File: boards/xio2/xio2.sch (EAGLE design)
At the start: 281 parts, among them J1 12401598E4#2A, Q1 BSS138, Q2 BSS138, X1 MINI-USB-UX60-MB-5ST, Y2 NX3225SA-12.000MHZ-STD-CSR-1

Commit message: Start work on the BGA STMH7
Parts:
- removed U$1: STM32H743XIH6, sjg-stm32:STM32H743XIH6
- added C99: 2.2uF, rcl:C-EUC0402K
- added R91, R92, R93: 33R, rcl:R-EU_R0402
- added TP14: (no value), microbuilder:TESTPOINTROUND0.5MM
- XIO: value STM32F429B-XIO -> STM32H743-XIO; device sjg-stm32:STM32F429B-XIO -> sjg-stm32:STM32H743-XIO
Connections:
- removed net N$100: U$1.P$35, U$1.P$36, U$1.P$37, U$1.P$38, U$1.P$39, U$1.P$40, U$1.P$41, U$1.P$42
- removed net N$101: U$1.P$52, U$1.P$53, U$1.P$55, U$1.P$56, U$1.P$57, U$1.P$58
- removed net N$102: U$1.P$69, U$1.P$70, U$1.P$71, U$1.P$72, U$1.P$73, U$1.P$74, U$1.P$75
- new net XIO_VCAP3: C99.1, XIO-POWER.VCAP3@A7
- new net XSPI_2_MISO: R75.2
- new net XSPI_2_MOSI: XIO-XSPI.PB15@T15
- new net XSPI_2_SCK: XIO-XSPI.PB13@U14
- net !RESET!: now also XIO-POWER.!RST!@K1; no longer XIO-POWER.!RST!@34
- net !SDRAM_CAS!: now also XIO-SDRAM.PG15@D6; no longer XIO-SDRAM.PG15@191
- net !SDRAM_RAS!: now also XIO-SDRAM.PF11@T7; no longer XIO-SDRAM.PF11@70
- net !SDRAM_WE!: now also XIO-SDRAM.PH5@P4; no longer XIO-SDRAM.PH5@49
- net +3V3: now also XIO-POWER.VBAT@B1, XIO-POWER.VDD33USB@F17, XIO-POWER.VDD@E11, XIO-POWER.VDD@E6, XIO-POWER.VDD@E9, XIO-POWER.VDD@F5, XIO-POWER.VDD@G13, XIO-POWER.VDD@G5, XIO-POWER.VDD@H13, XIO-POWER.VDD@H5, XIO-POWER.VDD@J13, XIO-POWER.VDD@K13, XIO-POWER.VDD@K5, XIO-POWER.VDD@L13, XIO-POWER.VDD@L5, XIO-POWER.VDD@M13, XIO-POWER.VDD@M5, XIO-POWER.VDD@N10, XIO-POWER.VDD@N11, XIO-POWER.VDD@N12, XIO-POWER.VDD@N7, XIO-POWER.VDD@N8, XIO-POWER.VDD@P17, XIO-POWER.VDDLDO@A6, XIO-POWER.VDDLDO@C17, XIO-POWER.VDDLDO@U12; no longer XIO-POWER.VBAT@6, XIO-POWER.VDD@103, XIO-POWER.VDD@115, XIO-POWER.VDD@124, XIO-POWER.VDD@15, XIO-POWER.VDD@150, XIO-POWER.VDD@158, XIO-POWER.VDD@171, XIO-POWER.VDD@185, XIO-POWER.VDD@204, XIO-POWER.VDD@26, XIO-POWER.VDD@39, XIO-POWER.VDD@52, XIO-POWER.VDD@59, XIO-POWER.VDD@73, XIO-POWER.VDD@83, XIO-POWER.VDD@94, XIO-POWER.VDDUSB@137
- net AGND: now also XIO-POWER.VREF-@N1, XIO-POWER.VSSA@P1
- net ARCH0: now also XIO-CFG.PG2@H16; no longer XIO-CFG.PG2@129
- net ARCH1: now also XIO-CFG.PG3@H15; no longer XIO-CFG.PG3@130
- net ARCH2: now also XIO-CFG.PG6@G15; no longer XIO-CFG.PG6@133
- net ARCH3: now also XIO-CFG.PG7@F16; no longer XIO-CFG.PG7@134
- net AUX_CTS: now also XIO-UART.PD11@R15; no longer XIO-SERIAL.PB13@105
- net AUX_RTS: now also XIO-UART.PD12@R16; no longer XIO-SERIAL.PB14@106
- net AUX_RX: now also XIO-UART.PB11@P12; no longer XIO-SERIAL.PB11@91
- net AUX_TX: now also XIO-UART.PB10@P11; no longer XIO-SERIAL.PB10@90
- net BOOT0: now also XIO-POWER.BOOT0@E8; no longer XIO-POWER.BOOT0@197
- net GND: now also C99.2, XIO-NC.F1, XIO-NC.F2, XIO-NC.G2, XIO-POWER.VSS@A1, XIO-POWER.VSS@A17, XIO-POWER.VSS@B2, XIO-POWER.VSS@B6, XIO-POWER.VSS@C10, XIO-POWER.VSS@C13, XIO-POWER.VSS@C16, XIO-POWER.VSS@G10, XIO-POWER.VSS@G11, XIO-POWER.VSS@G16, XIO-POWER.VSS@G7, XIO-POWER.VSS@G8, XIO-POWER.VSS@G9, XIO-POWER.VSS@H10, XIO-POWER.VSS@H11, XIO-POWER.VSS@H7, XIO-POWER.VSS@H8, XIO-POWER.VSS@H9, XIO-POWER.VSS@J10, XIO-POWER.VSS@J11, XIO-POWER.VSS@J16, XIO-POWER.VSS@J17, XIO-POWER.VSS@J3, XIO-POWER.VSS@J7, XIO-POWER.VSS@J8, XIO-POWER.VSS@J9, XIO-POWER.VSS@K10, XIO-POWER.VSS@K11, XIO-POWER.VSS@K15, XIO-POWER.VSS@K7, XIO-POWER.VSS@K8, XIO-POWER.VSS@K9, XIO-POWER.VSS@L10, XIO-POWER.VSS@L11, XIO-POWER.VSS@L15, XIO-POWER.VSS@L7, XIO-POWER.VSS@L8, XIO-POWER.VSS@L9, XIO-POWER.VSS@M15, XIO-POWER.VSS@N16, XIO-POWER.VSS@R4, XIO-POWER.VSS@R8, XIO-POWER.VSS@T12, XIO-POWER.VSS@U1, XIO-POWER.VSS@U17; no longer XIO-POWER.VSS@114, XIO-POWER.VSS@125, XIO-POWER.VSS@136, XIO-POWER.VSS@14, XIO-POWER.VSS@149, XIO-POWER.VSS@170, XIO-POWER.VSS@184, XIO-POWER.VSS@202, XIO-POWER.VSS@25, XIO-POWER.VSS@51, XIO-POWER.VSS@60, XIO-POWER.VSS@72, XIO-POWER.VSS@82, XIO-POWER.VSS@93, XIO-POWER.VSSA@40
- net LCD_B0: now also XIO-LCD.PJ12@D11; no longer XIO-VGA.PJ12@174
- net LCD_B1: now also XIO-LCD.PJ13@E10; no longer XIO-VGA.PJ13@175
- net LCD_B2: now also XIO-LCD.PJ14@D10; no longer XIO-VGA.PJ14@176
- net LCD_B3: now also XIO-LCD.PJ15@B10; no longer XIO-VGA.PJ15@177
- net LCD_B4: now also XIO-LCD.PK3@C8; no longer XIO-VGA.PK3@186
- net LCD_B5: now also XIO-LCD.PK4@B8; no longer XIO-VGA.PK4@187
- net LCD_B6: now also XIO-LCD.PK5@A8; no longer XIO-VGA.PK5@188
- net LCD_B7: now also XIO-LCD.PK6@C7; no longer XIO-VGA.PK6@189
- net LCD_G0: now also XIO-LCD.PJ7@N14; no longer XIO-VGA.PJ7@119
- net LCD_G1: now also XIO-LCD.PJ8@N13; no longer XIO-VGA.PJ8@120
- net LCD_G2: now also XIO-LCD.PJ9@M14; no longer XIO-VGA.PJ9@121
- net LCD_G3: now also XIO-LCD.PJ10@L14; no longer XIO-VGA.PJ10@122
- net LCD_G4: now also XIO-LCD.PJ11@K14; no longer XIO-VGA.PJ11@123
- net LCD_G5: now also XIO-LCD.PK0@J14; no longer XIO-VGA.PK0@126
- net LCD_G6: now also XIO-LCD.PK1@J15; no longer XIO-VGA.PK1@127
- net LCD_G7: now also XIO-LCD.PK2@H17; no longer XIO-VGA.PK2@128
- net LCD_HS: now also XIO-LCD.PI13@H2; no longer XIO-VGA.PI13@20
- net LCD_R0: now also XIO-LCD.PI15@P5; no longer XIO-VGA.PI15@64
- net LCD_R1: now also XIO-LCD.PJ0@N6; no longer XIO-VGA.PJ0@65
- net LCD_R2: now also XIO-LCD.PJ1@P6; no longer XIO-VGA.PJ1@66
- net LCD_R3: now also XIO-LCD.PJ2@T6; no longer XIO-VGA.PJ2@67
- net LCD_R4: now also XIO-LCD.PJ3@U6; no longer XIO-VGA.PJ3@68
- net LCD_R5: now also XIO-LCD.PJ4@U7; no longer XIO-VGA.PJ4@69
- net LCD_R6: now also XIO-LCD.PJ5@R12; no longer XIO-VGA.PJ5@95
- net LCD_R7: now also XIO-LCD.PJ6@N15; no longer XIO-VGA.PJ6@118
- net LCD_VS: now also XIO-LCD.PI12@H1; no longer XIO-VGA.PI12@19
- net MCU_CTS: now also XIO-UART.PD3@B12; no longer XIO-SERIAL.PD3@167
- net MCU_RTS: now also XIO-UART.PD4@A12; no longer XIO-SERIAL.PD4@168
- net MCU_RX: now also XIO-UART.PD6@B11; no longer XIO-SERIAL.PD6@172
- net MCU_TX: now also XIO-UART.PD5@A11; no longer XIO-SERIAL.PD5@169
- net MEM0: now also XIO-CFG.PG10@A9; no longer XIO-CFG.PG10@179
- net MEM1: now also XIO-CFG.PG11@B9; no longer XIO-CFG.PG11@180
- net N$1: now also XIO-POWER.PH1@J2; no longer XIO-POWER.PH1@33
- net N$13: now also XIO-LED.PC13@E3; no longer XIO-LED.PD11@111
- net N$14: now also XIO-LED.PC14@C2; no longer XIO-LED.PD12@112
- net N$15: now also XIO-LED.PC15@C1; no longer XIO-LED.PD13@113
- net N$2: now also XIO-POWER.PH0@J1; no longer XIO-POWER.PH0@32
- net N$57: now also XIO-SPI.PE2@C3; no longer XIO-SPI.PE2@1
- net N$61: now also XIO-SPI.PE6@E5; no longer XIO-SPI.PE6@5
- net N$64: now also XIO-USB.PA15@A14; no longer XIO-USB.PA15@160
- net N$65: now also XIO-USB.PD7@C11; no longer XIO-USB.PD7@173
- net N$72: now also XIO-XSPI.PB14@U15; no longer XIOG$1.PB4@193
- net N$73: now also XIO-XSPI.PB4@B7; no longer XIOG$1.PF8@29
- net N$74: now also XIO-XSPI.PF7@K3; no longer XIOG$1.PG12@181
- net N$75: now also XIO-XSPI.PA6@R3; no longer XIOG$1.PA5@54
- net N$76: now also R91.1, XIO-XSPI.PF9@L4; no longer R74.1, XIOG$1.PA7@56
- net N$79: now also R92.1, XIO-XSPI.PG13@D9; no longer R80.1, XLX-B1.IO_L74P_AWAKE_1
- net N$85: now also XIO-UNUSED.PA2@N3; no longer XIO-UNUSED.PA2@45
- net N$86: now also XIO-UNUSED.PA3@U2; no longer XIO-UNUSED.PA3@50
- net N$87: now also XIO-UNUSED.PA4@U3; no longer XIO-UNUSED.PA4@53
- net N$88: now also XIO-UNUSED.PC6@F14; no longer XIO-UNUSED.PC5@58
- net N$89: now also XIO-UNUSED.PD13@R17; no longer XIO-UNUSED.PC6@138
- net N$90: now also XIO-UNUSED.PE3@D3; no longer XIO-UNUSED.PC13@8
- net N$91: now also XIO-UNUSED.PE4@D2; no longer XIO-UNUSED.PC14@9
- net N$92: now also XIO-UNUSED.PF6@K2; no longer XIO-UNUSED.PC15@10
- net N$93: now also XIO-UNUSED.PF10@L3; no longer XIO-UNUSED.PE3@2
- net N$94: now also XIO-UNUSED.PG9@A10; no longer XIO-UNUSED.PE4@3
- net N$95: now also XIO-UNUSED.PA0_C@T1; no longer XIO-UNUSED.PF6@27
- net N$96: now also XIO-UNUSED.PA1_C@T2; no longer XIO-UNUSED.PF10@31
- net N$97: now also XIO-UNUSED.PC2_C@R1; no longer XIO-UNUSED.PG9@178
- net N$98: now also R93.1, XIO-XSPI.PG14@D8; no longer U$1.P$1, U$1.P$2, U$1.P$3, U$1.P$4, U$1.P$5, U$1.P$6, U$1.P$7, U$1.P$8, U$1.P$9
- net N$99: now also TP14.P$1, XIO-UNUSED.PC3_C@R2; no longer U$1.P$18, U$1.P$19, U$1.P$20, U$1.P$21, U$1.P$22, U$1.P$23, U$1.P$24, U$1.P$25
- net PDR_ON: now also XIO-POWER.PDR_ON@E7; no longer XIO-POWER.PDR_ON@203
- net PID0: now also XIO-CFG.PI8@E4; no longer XIO-CFG.PI8@7
- net PID1: now also XIO-CFG.PI11@F4; no longer XIO-CFG.PI11@13
- net PID2: now also XIO-CFG.PI14@H3; no longer XIO-CFG.PI14@21
- net SD0: now also XIO-SDCARD.PC8@E13; no longer XIO-SDCARD.PC8@140
- net SD1: now also XIO-SDCARD.PC9@E14; no longer XIO-SDCARD.PC9@141
- net SD2: now also XIO-SDCARD.PC10@A13; no longer XIO-SDCARD.PC10@161
- net SD3: now also XIO-SDCARD.PC11@B13; no longer XIO-SDCARD.PC11@162
- net SDCD: now also XIO-SDCARD.PC7@F13; no longer XIO-SDCARD.PC7@139
- net SDCLK: now also XIO-SDCARD.PC12@C12; no longer XIO-SDCARD.PC12@163
- net SDCMD: now also XIO-SDCARD.PD2@D12; no longer XIO-SDCARD.PD2@166
- net SDRAM_A0: now also XIO-SDRAM.PF0@G4; no longer XIO-SDRAM.PF0@16
- net SDRAM_A1: now also XIO-SDRAM.PF1@G3; no longer XIO-SDRAM.PF1@17
- net SDRAM_A10: now also XIO-SDRAM.PG0@T8; no longer XIO-SDRAM.PG0@77
- net SDRAM_A11: now also XIO-SDRAM.PG1@U8; no longer XIO-SDRAM.PG1@78
- net SDRAM_A2: now also XIO-SDRAM.PF2@G1; no longer XIO-SDRAM.PF2@18
- net SDRAM_A3: now also XIO-SDRAM.PF3@H4; no longer XIO-SDRAM.PF3@22
- net SDRAM_A4: now also XIO-SDRAM.PF4@J5; no longer XIO-SDRAM.PF4@23
- net SDRAM_A5: now also XIO-SDRAM.PF5@J4; no longer XIO-SDRAM.PF5@24
- net SDRAM_A6: now also XIO-SDRAM.PF12@R7; no longer XIO-SDRAM.PF12@71
- net SDRAM_A7: now also XIO-SDRAM.PF13@P7; no longer XIO-SDRAM.PF13@74
- net SDRAM_A8: now also XIO-SDRAM.PF14@P8; no longer XIO-SDRAM.PF14@75
- net SDRAM_A9: now also XIO-SDRAM.PF15@R9; no longer XIO-SDRAM.PF15@76
- net SDRAM_BA0: now also XIO-SDRAM.PG4@H14; no longer XIO-SDRAM.PG4@131
- net SDRAM_BA1: now also XIO-SDRAM.PG5@G14; no longer XIO-SDRAM.PG5@132
- net SDRAM_CLK: now also XIO-SDRAM.PG8@F15; no longer XIO-SDRAM.PG8@135
- net SDRAM_D0: now also XIO-SDRAM.PD14@P16; no longer XIO-SDRAM.PD14@116
- net SDRAM_D1: now also XIO-SDRAM.PD15@P15; no longer XIO-SDRAM.PD15@117
- net SDRAM_D10: now also XIO-SDRAM.PE13@T10; no longer XIO-SDRAM.PE13@87
- net SDRAM_D11: now also XIO-SDRAM.PE14@U10; no longer XIO-SDRAM.PE14@88
- net SDRAM_D12: now also XIO-SDRAM.PE15@R11; no longer XIO-SDRAM.PE15@89
- net SDRAM_D13: now also XIO-SDRAM.PD8@U16; no longer XIO-SDRAM.PD8@108
- net SDRAM_D14: now also XIO-SDRAM.PD9@T17; no longer XIO-SDRAM.PD9@109
- net SDRAM_D15: now also XIO-SDRAM.PD10@T16; no longer XIO-SDRAM.PD10@110
- net SDRAM_D16: now also XIO-SDRAM.PH8@T13; no longer XIO-SDRAM.PH8@98
- net SDRAM_D17: now also XIO-SDRAM.PH9@R13; no longer XIO-SDRAM.PH9@99
- net SDRAM_D18: now also XIO-SDRAM.PH10@P13; no longer XIO-SDRAM.PH10@100
- net SDRAM_D19: now also XIO-SDRAM.PH11@P14; no longer XIO-SDRAM.PH11@101
- net SDRAM_D2: now also XIO-SDRAM.PD0@D13; no longer XIO-SDRAM.PD0@164
- net SDRAM_D20: now also XIO-SDRAM.PH12@R14; no longer XIO-SDRAM.PH12@102
- net SDRAM_D21: now also XIO-SDRAM.PH13@D16; no longer XIO-SDRAM.PH13@151
- net SDRAM_D22: now also XIO-SDRAM.PH14@B17; no longer XIO-SDRAM.PH14@152
- net SDRAM_D23: now also XIO-SDRAM.PH15@B16; no longer XIO-SDRAM.PH15@153
- net SDRAM_D24: now also XIO-SDRAM.PI0@A16; no longer XIO-SDRAM.PI0@154
- net SDRAM_D25: now also XIO-SDRAM.PI1@A15; no longer XIO-SDRAM.PI1@155
- net SDRAM_D26: now also XIO-SDRAM.PI2@B15; no longer XIO-SDRAM.PI2@156
- net SDRAM_D27: now also XIO-SDRAM.PI3@C14; no longer XIO-SDRAM.PI3@157
- net SDRAM_D28: now also XIO-SDRAM.PI6@A2; no longer XIO-SDRAM.PI6@207
- net SDRAM_D29: now also XIO-SDRAM.PI7@B3; no longer XIO-SDRAM.PI7@208
- net SDRAM_D3: now also XIO-SDRAM.PD1@E12; no longer XIO-SDRAM.PD1@165
- net SDRAM_D30: now also XIO-SDRAM.PI9@E2; no longer XIO-SDRAM.PI9@11
- net SDRAM_D31: now also XIO-SDRAM.PI10@F3; no longer XIO-SDRAM.PI10@12
- net SDRAM_D4: now also XIO-SDRAM.PE7@U9; no longer XIO-SDRAM.PE7@79
- net SDRAM_D5: now also XIO-SDRAM.PE8@T9; no longer XIO-SDRAM.PE8@80
- net SDRAM_D6: now also XIO-SDRAM.PE9@P9; no longer XIO-SDRAM.PE9@81
- net SDRAM_D7: now also XIO-SDRAM.PE10@N9; no longer XIO-SDRAM.PE10@84
- net SDRAM_D8: now also XIO-SDRAM.PE11@P10; no longer XIO-SDRAM.PE11@85
- net SDRAM_D9: now also XIO-SDRAM.PE12@R10; no longer XIO-SDRAM.PE12@86
- net SDRAM_DQM0: now also XIO-SDRAM.PE0@C4; no longer XIO-SDRAM.PE0@200
- net SDRAM_DQM1: now also XIO-SDRAM.PE1@B4; no longer XIO-SDRAM.PE1@201
- net SDRAM_DQM2: now also XIO-SDRAM.PI4@A4; no longer XIO-SDRAM.PI4@205
- net SDRAM_DQM3: now also XIO-SDRAM.PI5@A3; no longer XIO-SDRAM.PI5@206
- net SPI_IRQ0: now also XIO-SPI.PC0@L2; no longer XIO-SPI.PC0@35
- net SPI_IRQ1: now also XIO-SPI.PC1@M2; no longer XIO-SPI.PC1@36
- net SPI_IRQ2: now also XIO-SPI.PC2@M3; no longer XIO-SPI.PC2@37
- net SPI_IRQ3: now also XIO-SPI.PC3@M4; no longer XIO-SPI.PC3@38
- net SPI_IRQ4: now also XIO-SPI.PC4@T4; no longer XIO-SPI.PC4@57
- net SPI_MISO: now also XIO-SPI.PE5@D1; no longer XIO-SPI.PE5@4
- net SPI_MUX_IN: now also XIO-SPI.PK7@D7; no longer XIO-SPI.PK7@190
- net SPI_SS0: now also XIO-SPI.PH2@N2; no longer XIO-SPI.PH2@46
- net SPI_SS1: now also XIO-SPI.PH3@P2; no longer XIO-SPI.PH3@47
- net SPI_SS2: now also XIO-SPI.PH4@P3; no longer XIO-SPI.PH4@48
- net SPI_SS3: now also XIO-SPI.PH6@T11; no longer XIO-SPI.PH6@96
- net SPI_SS4: now also XIO-SPI.PH7@U13; no longer XIO-SPI.PH7@97
- net STMB0: now also XIO-UNUSED.PB0@U5; no longer XIO-UNUSED.PB0@61
- net STMB1: now also XIO-UNUSED.PB1@T5; no longer XIO-UNUSED.PB1@62
- net STMB12: now also XIO-UNUSED.PB12@T14; no longer XIO-UNUSED.PB12@104
- net STMB15: now also XIO-UNUSED.PC5@U4; no longer SLOT0.B22, SLOT1.B22, SLOT2.B22, SLOT3.B22, SLOT4.B22, XIO-UNUSED.PB15@107
- net STMB2: now also XIO-UNUSED.PB2@R6; no longer XIO-UNUSED.PB2@63
- net STMB6: now also XIO-UNUSED.PB6@B5; no longer XIO-UNUSED.PB6@195
- net STMB7: now also XIO-UNUSED.PB7@C5; no longer XIO-UNUSED.PB7@196
- net STMB8: now also XIO-UNUSED.PB8@D5; no longer XIO-UNUSED.PB8@198
- net STMB9: now also XIO-UNUSED.PB9@D4; no longer XIO-UNUSED.PB9@199
- net XIO_RX: now also XIO-POWER.PA1@N4; no longer XIO-POWER.PA1@44
- net XIO_SWDCLK: now also XIO-POWER.PA14@B14; no longer XIO-POWER.PA14@159
- net XIO_SWDIO: now also XIO-POWER.PA13@C15; no longer XIO-POWER.PA13@147
- net XIO_TX: now also XIO-POWER.PA0@N5; no longer XIO-POWER.PA0@43
- net XIO_USB_ID: now also XIO-USB.PA10@D14; no longer XIO-USB.PA10@144
- net XIO_USB_N: now also XIO-USB.PA11@E17; no longer XIO-USB.PA11@145
- net XIO_USB_P: now also XIO-USB.PA12@E16; no longer XIO-USB.PA12@146
- net XIO_USB_VBUS: now also XIO-USB.PA9@D15; no longer XIO-USB.PA9@143
- net XIO_VCAP1: now also C18.1, XIO-POWER.VCAP1@U11; no longer C17.1, XIO-POWER.VCAP1@92
- net XIO_VCAP2: now also C17.1, XIO-POWER.VCAP2@D17; no longer C18.1, XIO-POWER.VCAP2@148
- net XIO_VDDA: now also XIO-POWER.VDDA@L1, XIO-POWER.VREF+@M1; no longer XIO-POWER.VDDA@42, XIO-POWER.VREF+@41
- net XSPI_1_MISO: now also R73.2; no longer R80.2, XIOG$1.PA6@55
- net XSPI_1_MOSI: now also XIO-XSPI.PA7@R5; no longer XLX-B1.IO_L74N_DOUT_BUSY_1
- net XSPI_1_SCK: now also R80.2, XIO-XSPI.PA5@T3; no longer R73.2, XLX-B1.IO_L47N_1
- net XSPI_3_MISO: now also R76.2; no longer R75.2
- net XSPI_3_MOSI: now also XIO-XSPI.PB5@A5; no longer XIOG$1.PB5@194
- net XSPI_3_SCK: now also XIO-XSPI.PB3@C6; no longer XIOG$1.PB3@192
- net XSPI_5_MISO: now also XIO-XSPI.PF8@K4; no longer R76.2
- net XSPI_5_MOSI: now also R91.2; no longer XIOG$1.PF9@30
- net XSPI_5_SCK: now also R77.2; no longer XIOG$1.PF7@28
- net XSPI_6_MISO: now also XIO-XSPI.PG12@C9; no longer R77.2
- net XSPI_6_MOSI: now also R93.2; no longer XIOG$1.PG14@183
- net XSPI_6_SCK: now also R92.2; no longer XIOG$1.PG13@182
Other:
- note added: "2.5v"
- note added: "3 SPI channels at 150 MBit/s and 2 SPI channels at 100 MBit/s (level-translated)"
- note added: "@100 MHz"
- note added: "@400"
- note added: "Board Config"
- note added: "NC Pins"
- note added: "SPI1, SPI2, SPI3 to be used with FPGA as master. SPI5, SPI6 to be used with STM as master Resistors sited close to source signal"
- note added: "SPI1,2,3 @ 150 MHz"
- note added: "SPI5,6 @ 100MHz"
- note added: "STM32H743 (XIO) (TFBGA 240+25)"
- note added: "TO DO - check USB VBUS is ok ? - verify FPGA configuration pins - check DONE_2 on the FPGA - any more signals on the slots bus ? - Check milling layer is acceptable for hole - maybe put some support for daughterboard on FPGA - Move to 0201 parts for caps/resistors - Add card-present lines to STM"
- note removed: "3 SPI channels at 45 MBit/s and 1 SPI channel at 22.5 MBit/s"
- note removed: "@180"
- note removed: "@22.5"
- note removed: "@45"
- note removed: "SPI1, SPI5, SPI6 to be used with FPGA as master. SPI3 to be used with STM as master Resistors sited close to source signal"
- note removed: "SPI1,5,6"
- note removed: "SPI3"
- note removed: "STM32F429 (XIO) (PQ208)"
- note removed: "TO DO - check USB VBUS is ok ? - verify FPGA configuration pins - check DONE_2 on the FPGA - any more signals on the slots bus ? - Check milling layer is acceptable for hole - maybe put some support for daughterboard on FPGA"
- moved on the sheet: ARCH_ID, C1, C10, C11, C12, C13, C14, C15, C16, C17, C18, C2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

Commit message: Test out the BGA routability
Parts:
- C10, C13, C14, C15, C16, C17, C18, C2, C26, C27, C28, C29, C3, C31, C32, C33, C4, C5, C6, C7, C8, C9, C99: device rcl:C-EUC0402K -> rcl:C-EUC0201
- R1, R21, R26, R27, R5, R53, R72, R73, R75, R76, R77, R91, R92, R93: device rcl:R-EU_R0402 -> rcl:R-EU_R0201

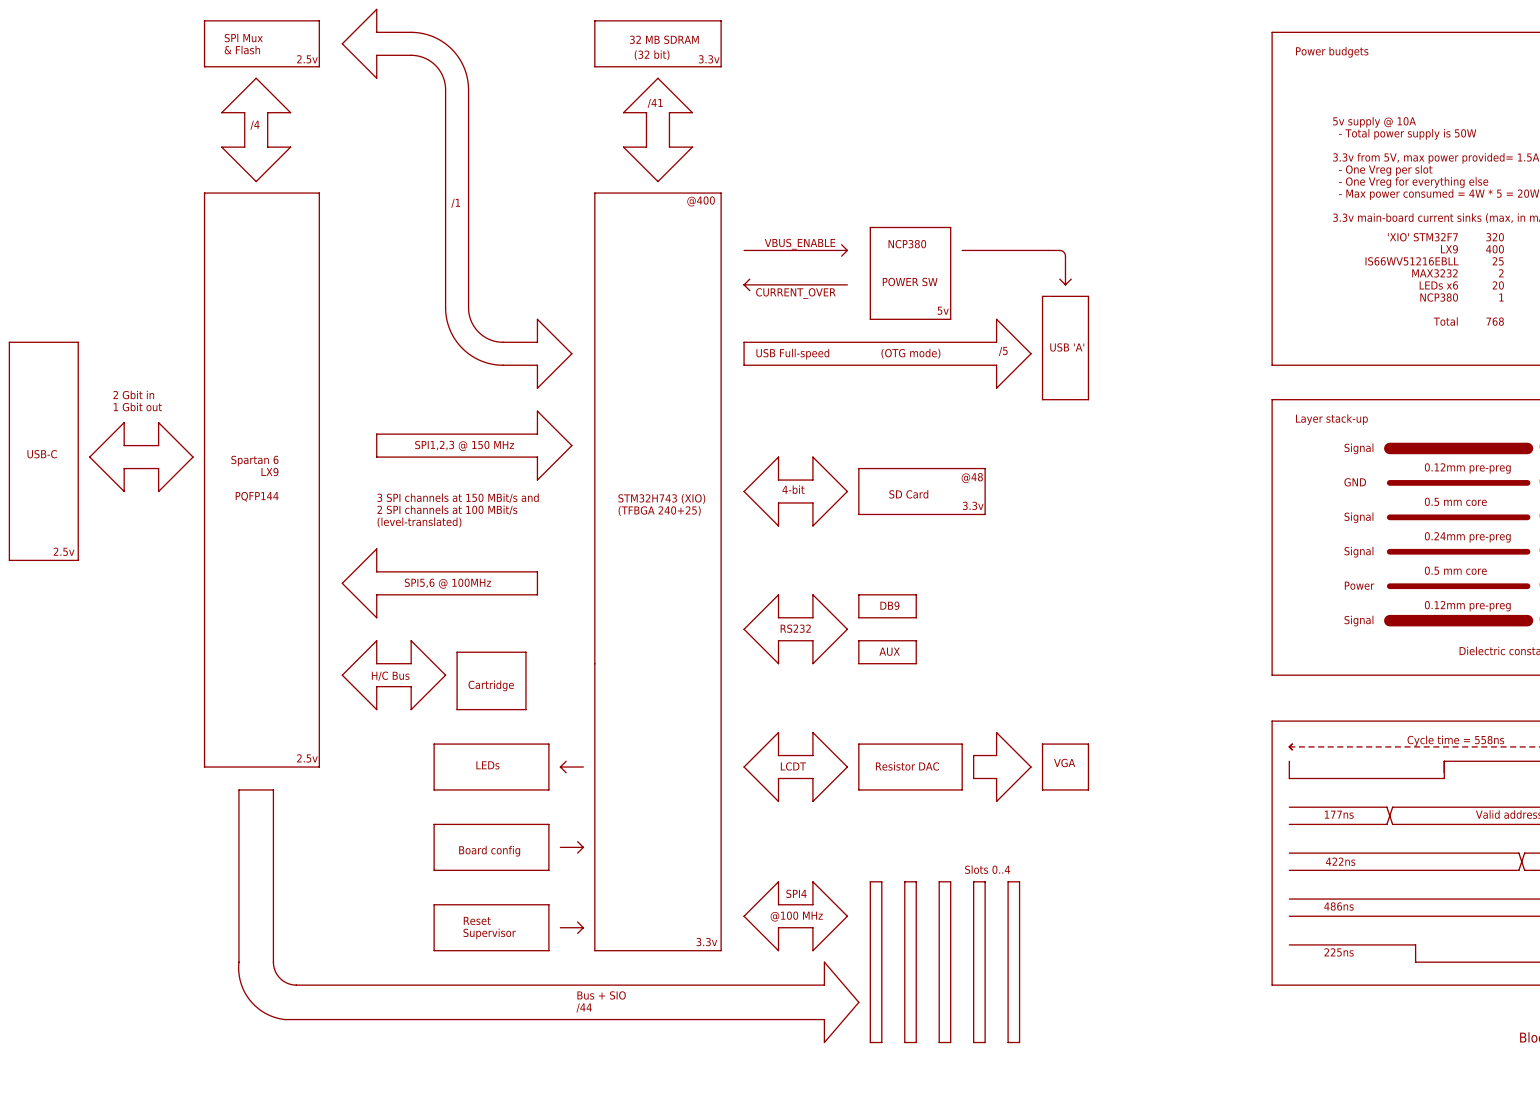
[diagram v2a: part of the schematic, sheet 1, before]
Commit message: Update the top-level block diagram to suit the new design
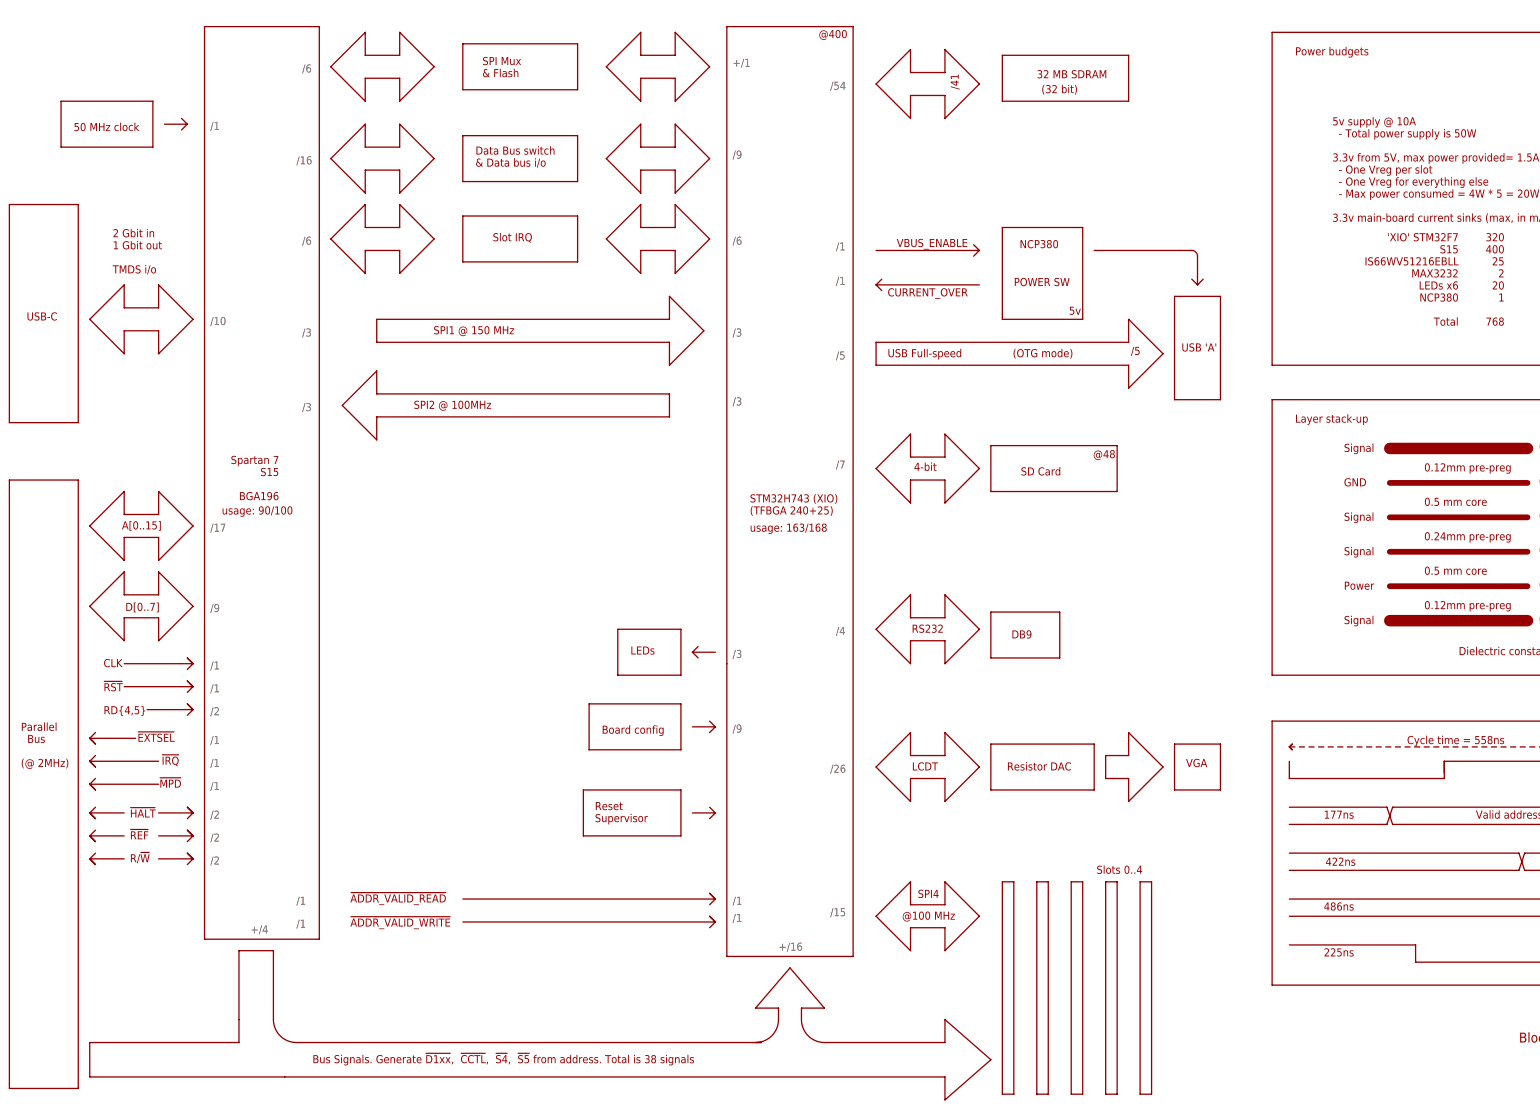
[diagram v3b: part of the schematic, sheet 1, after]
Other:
- note added: "!ADDR_VALID_READ!"
- note added: "!ADDR_VALID_WRITE!"
- note added: "!EXTSEL!"
- note added: "!HALT!"
- note added: "!IRQ!"
- note added: "!MPD!"
- note added: "!REF!"
- note added: "!RST!"
- note added: "'XIO' STM32F7 S15 IS66WV51216EBLL MAX3232 LEDs x6 NCP380 Total"
- note added: "+/1"
- note added: "+/16"
- note added: "+/4"
- note added: "/10"
- note added: "/15"
- note added: "/16"
- note added: "/17"
- note added: "/2"
- note added: "/26"
- note added: "/3"
- note added: "/54"
- note added: "/6"
- note added: "/7"
- note added: "/9"
- note added: "2 Gbit in 1 Gbit out TMDS i/o"
- note added: "50 MHz clock"
- note added: "A[0..15]"
- note added: "Bus Signals. Generate !D1xx!, !CCTL!, !S4!, !S5! from address. Total is 38 signals"
- note added: "D[0..7]"
- note added: "Data Bus switch & Data bus i/o"
- note added: "Parallel Bus (@ 2MHz)"
- note added: "R/!W!"
- note added: "RD{4,5}"
- note added: "SPI1 @ 150 MHz"
- note added: "SPI2 @ 100MHz"
- note added: "Slot IRQ"
- note added: "Spartan 7 S15 BGA196"
- note added: "usage: 163/168"
- note added: "usage: 90/100"
- note removed: "'XIO' STM32F7 LX9 IS66WV51216EBLL MAX3232 LEDs x6 NCP380 Total"
- note removed: "2 Gbit in 1 Gbit out"
- note removed: "2.5v"
- note removed: "3 SPI channels at 150 MBit/s and 2 SPI channels at 100 MBit/s (level-translated)"
- note removed: "3.3v"
- note removed: "AUX"
- note removed: "Bus + SIO /44"
- note removed: "Cartridge"
- note removed: "H/C Bus"
- note removed: "SPI1,2,3 @ 150 MHz"
- note removed: "SPI5,6 @ 100MHz"
- note removed: "Spartan 6 LX9 PQFP144"
- note removed: "[12]"
- note removed: "[16]"

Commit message: Start integrating the S7
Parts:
- removed AUX-SIO: (no value), pinhead:PINHD-1X6
- removed C88: 0.47uF, rcl:C-EUC0402K
- removed JP2: (no value), pinhead:PINHD-2X7
- removed R81, R82, R86, R87: 33R, rcl:R-EU_R0402
- removed RESET_XLX: 1825910-6, SparkFun:TAC_SWITCHPTH
- removed TP1, TP10, TP11, TP12, TP13, TP14, TP2, TP3, TP4, TP5, TP6, TP7, TP8, TP9: (no value), microbuilder:TESTPOINTROUND0.5MM
- removed XLX-: 6SLX9TQG144, xilinx_devices_V6:6SLX9TQG144
- added C101: 100uF, rcl:C-EUC1210
- added C102: 4.7uF, rcl:C-EUC0805
- added C104: 0.47uF, rcl:C-EUC0603
- added RESET_S7: 1825910-6, SparkFun:TAC_SWITCHPTH
- added U$1: XC7S15, sjg-xilinx:XC7S15
- added VREG1_0: AP7363, sjg-power:AP7363
- C30: value 0.1uF -> 0.47uF; device rcl:C-EUC0402K -> rcl:C-EUC0603
- C36, C47, C48, C49, C50, C51, C58, C84: value 4.7uF -> 0.47uF; device rcl:C-EUC0402K -> rcl:C-EUC0603
- C52: value 0.47uF -> 47uF; device rcl:C-EUC0402K -> rcl:C-EUC1210
- C59, C74, C75: device rcl:C-EUC0402K -> rcl:C-EUC0805
- C73: value 0.47uF -> 100uF; device rcl:C-EUC0402K -> rcl:C-EUC1210
- C76, C78, C79, C82: value 0.47uF -> 4.7uF; device rcl:C-EUC0402K -> rcl:C-EUC0805
- C77: value 4.7uF -> 100uF; device rcl:C-EUC0402K -> rcl:C-EUC1210
- C80, C87: value 4.7uF -> 10uF
- C83, C85, C86: device rcl:C-EUC0402K -> rcl:C-EUC0603
- C89, C90, C91, C92, C94: device rcl:C-EUC0402K -> rcl:C-EUC0201
- JP1: device pinhead:PINHD-2X8 -> pinhead:PINHD-2X20/90
- R10, R11, R12, R13, R19, R20, R22, R23, R24, R25, R28, R29, R30, R31, R32, R33, R34, R35, R42, R43, R44, R45, R46, R47, R48, R49: device rcl:R-EU_R0402 -> rcl:R-EU_R0201
- R52: value 680R -> 33R
- R60: value 4.7K -> 33R
- R66: value 4.7K -> 200R
- R68: value 33R -> 100R
- R69, R78, R79: value 33R -> 4.7K
- renumbered VREG1_2 to VREG1_8
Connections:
- removed net 1.2V: C36.1, C73.1, C74.1, C75.1, C93.1, R67.1, VREG1_8.TAB, VREG1_8.VOUT, XLX-BVCCINT.VCCINT@0, XLX-BVCCINT.VCCINT@1, XLX-BVCCINT.VCCINT@2, XLX-BVCCINT.VCCINT@3, XLX-BVCCINT.VCCINT@4
- removed net AUX_CTS: AUX-SIO.2, XIO-UART.PD11@R15
- removed net AUX_RTS: AUX-SIO.5, XIO-UART.PD12@R16
- removed net AUX_RX: AUX-SIO.3, XIO-UART.PB11@P12
- removed net AUX_TX: AUX-SIO.4, XIO-UART.PB10@P11
- removed net CBUS_!CCTL!: CARTRIDGE.!CCTL!@15, LVL_AHI.B6@16
- removed net CBUS_!S4!: CARTRIDGE.!S4!@1, LVL_AHI.B7@15
- removed net CBUS_!S5!: CARTRIDGE.!S5!@12, LVL_AHI.B8@14
- removed net CBUS_A0: CARTRIDGE.A0@5, LVL_ALO.B1@21
- removed net CBUS_A1: CARTRIDGE.A1@4, LVL_ALO.B2@20
- removed net CBUS_A10: CARTRIDGE.A10@P, LVL_AHI.B3@19
- removed net CBUS_A11: CARTRIDGE.A11@N, LVL_AHI.B4@18
- removed net CBUS_A12: CARTRIDGE.A12@K, LVL_AHI.B5@17
- removed net CBUS_A2: CARTRIDGE.A2@3, LVL_ALO.B3@19
- removed net CBUS_A3: CARTRIDGE.A3@2, LVL_ALO.B4@18
- removed net CBUS_A4: CARTRIDGE.A4@C, LVL_ALO.B5@17
- removed net CBUS_A5: CARTRIDGE.A5@D, LVL_ALO.B6@16
- removed net CBUS_A6: CARTRIDGE.A6@E, LVL_ALO.B7@15
- removed net CBUS_A7: CARTRIDGE.A7@F, LVL_ALO.B8@14
- removed net CBUS_A8: CARTRIDGE.A8@H, LVL_AHI.B1@21
- removed net CBUS_A9: CARTRIDGE.A9@J, LVL_AHI.B2@20
- removed net CBUS_B02: CARTRIDGE.B02@S, LVL_CLK.B@4
- removed net CBUS_D0: CARTRIDGE.D0@10, LVL_D.B1@21
- removed net CBUS_D1: CARTRIDGE.D1@9, LVL_D.B2@20
- removed net CBUS_D2: CARTRIDGE.D2@8, LVL_D.B3@19
- removed net CBUS_D3: CARTRIDGE.D3@L, LVL_D.B4@18
- removed net CBUS_D4: CARTRIDGE.D4@6, LVL_D.B5@17
- removed net CBUS_D5: CARTRIDGE.D5@7, LVL_D.B6@16
- removed net CBUS_D6: CARTRIDGE.D6@11, LVL_D.B7@15
- removed net CBUS_D7: CARTRIDGE.D7@M, LVL_D.B8@14
- removed net CBUS_R/!W!: CARTRIDGE.R/!W!@R, LVL_RW.B@4
- removed net FBUS0: JP1.14, XLX-B0.IO_L36P_GCLK15_0
- removed net FBUS1: JP1.12, XLX-B0.IO_L36N_GCLK14_0
- removed net FBUS10: JP1.7, XLX-B0.IO_L65N_SCP2_0
- removed net FBUS11: JP1.5, XLX-B0.IO_L66P_SCP1_0
- removed net FBUS12: JP1.3, XLX-B0.IO_L66N_SCP0_0
- removed net FBUS13: JP2.1, XLX-B1.IO_L1P_1
- removed net FBUS14: JP2.3, XLX-B1.IO_L1N_VREF_1
- removed net FBUS15: JP2.5, XLX-B1.IO_L33N_1
- removed net FBUS16: JP2.7, XLX-B1.IO_L34P_1
- removed net FBUS17: JP2.9, XLX-B1.IO_L34N_1
- removed net FBUS18: JP2.11, XLX-B1.IO_L40P_GCLK11_1
- removed net FBUS19: JP2.2, XLX-B1.IO_L42P_GCLK7_1
- removed net FBUS2: JP1.10, XLX-B0.IO_L37N_GCLK12_0
- removed net FBUS20: JP2.4, XLX-B1.IO_L42N_GCLK6_TRDY1_1
- removed net FBUS21: JP2.6, XLX-B1.IO_L43P_GCLK5_1
- removed net FBUS22: JP2.8, XLX-B1.IO_L43N_GCLK4_1
- removed net FBUS23: JP2.10, XLX-B1.IO_L45P_1
- removed net FBUS24: JP2.12, XLX-B1.IO_L45N_1
- removed net FBUS3: JP1.8, XLX-B0.IO_L62P_0
- removed net FBUS4: JP1.6, XLX-B0.IO_L62N_VREF_0
- removed net FBUS5: JP1.4, XLX-B0.IO_L63P_SCP7_0
- removed net FBUS6: JP1.2, XLX-B0.IO_L63N_SCP6_0
- removed net FBUS7: JP1.13, XLX-B0.IO_L64P_SCP5_0
- removed net FBUS8: JP1.11, XLX-B0.IO_L64N_SCP4_0
- removed net FBUS9: JP1.9, XLX-B0.IO_L65P_SCP3_0
- removed net HBUS_!CCTL!: LVL_AHI.A6@8, XLX-B2.IO_L64N_D9_2
- removed net HBUS_!S4!: LVL_AHI.A7@9, XLX-B2.IO_L48N_RDWR_B_VREF_2
- removed net HBUS_!S5!: LVL_AHI.A8@10, XLX-B2.IO_L48P_D7_2
- removed net HBUS_DDIR: LVL_D.DIR@2, XLX-B0.IO_L1N_VREF_0
- removed net N$78: R78.1, XLX-B1.IO_L32N_1
- removed net N$80: R86.1, XLX-B1.IO_L46P_1
- removed net N$81: R87.1, XLX-B1.IO_L47P_1
- removed net N$85: TP1.P$1, XIO-UNUSED.PA2@N3
- removed net N$86: TP2.P$1, XIO-UNUSED.PA3@U2
- removed net N$87: TP3.P$1, XIO-UNUSED.PA4@U3
- removed net N$88: TP4.P$1, XIO-UNUSED.PC6@F14
- removed net N$89: TP5.P$1, XIO-UNUSED.PD13@R17
- removed net N$90: TP6.P$1, XIO-UNUSED.PE3@D3
- removed net N$91: TP7.P$1, XIO-UNUSED.PE4@D2
- removed net N$92: TP8.P$1, XIO-UNUSED.PF6@K2
- removed net N$93: TP9.P$1, XIO-UNUSED.PF10@L3
- removed net N$94: TP10.P$1, XIO-UNUSED.PG9@A10
- removed net N$95: TP11.P$1, XIO-UNUSED.PA0_C@T1
- removed net N$96: TP12.P$1, XIO-UNUSED.PA1_C@T2
- removed net N$97: TP13.P$1, XIO-UNUSED.PC2_C@R1
- removed net N$99: TP14.P$1, XIO-UNUSED.PC3_C@R2
- removed net STMB15: XIO-UNUSED.PC5@U4
- new net VCCAUX: C51.1, C52.1, C58.1, C59.1, C93.1, R67.1, U$1-PWR.VCCAUX@F10, U$1-PWR.VCCAUX@H10, U$1-PWR.VCCAUX@K10, U$1-PWR.VCCAUX@L9, VREG1_8.TAB, VREG1_8.VOUT
- new net VCCINT: C101.1, C102.1, C104.1, C30.1, C36.1, C73.1, C74.1, C75.1, C87.1, U$1-PWR.VCCBRAM@E5, U$1-PWR.VCCBRAM@G5, U$1-PWR.VCCBRAM@J5, U$1-PWR.VCCINT@D6, U$1-PWR.VCCINT@D8, U$1-PWR.VCCINT@E7, U$1-PWR.VCCINT@E9, U$1-PWR.VCCINT@F6, U$1-PWR.VCCINT@G9, U$1-PWR.VCCINT@H6, U$1-PWR.VCCINT@J9, U$1-PWR.VCCINT@K6, U$1-PWR.VCCINT@K8, VREG1_0.OUT@3
- net +3V3: now also R69.2, R78.2, R79.2, U$1-CFG.M0_0@M7, U$1-CFG.VCCO_0@N6, U$1-CFG.VCCO_0@N8; no longer AUX-SIO.1, C51.1, C52.1, C58.1, C59.1, C80.1, C87.1, C88.1, JP1.15, JP2.14, R52.1, R60.2, XLX-B0.VCCO_0@0, XLX-B0.VCCO_0@1, XLX-B0.VCCO_0@2, XLX-B1.VCCO_1@0, XLX-B1.VCCO_1@1, XLX-B1.VCCO_1@2, XLX-B2.IO_L1N_M0_CMPMISO_2, XLX-B2.VCCO_2@0, XLX-B2.VCCO_2@1, XLX-B3.VCCO_3@0, XLX-B3.VCCO_3@1, XLX-B3.VCCO_3@2, XLX-BVCCAUX.VCCAUX@0, XLX-BVCCAUX.VCCAUX@1, XLX-BVCCAUX.VCCAUX@2, XLX-BVCCAUX.VCCAUX@3, XLX-BVCCAUX.VCCAUX@4
- net +5V: now also C80.1, VREG1_0.IN@1
- net FLASH_CLK: now also R52.2; no longer R68.2
- net FLASH_CS: now also U$1-CFG.IO_L2N_T0_D03_14@C10; no longer XLX-B2.IO_L65N_CSO_B_2
- net FLASH_D0: now also R60.2; no longer R69.2
- net FLASH_D1: now also U$1-CFG.IO_L15N_T2_DQS_DOUT_CSO_B_14@L14; no longer XLX-B2.IO_L3P_D0_DIN_MISO_MISO1_2
- net FLASH_D2: now also U$1-CFG.IO_L2P_T0_D02_14@D10; no longer XLX-B2.IO_L12P_D1_MISO2_2
- net FLASH_D3: now also U$1-CFG.IO_L1N_T0_D01_DIN_14@B12; no longer XLX-B2.IO_L12N_D2_MISO3_2
- net GND: now also C101.2, C102.2, C104.2, RESET_S7.1, RESET_S7.2, U$1-CFG.DXN_0@J7, U$1-CFG.DXP_0@J8, U$1-CFG.M1_0@M8, U$1-CFG.M2_0@M9, U$1-PWR.GND@A1, U$1-PWR.GND@A11, U$1-PWR.GND@A14, U$1-PWR.GND@A6, U$1-PWR.GND@A9, U$1-PWR.GND@B4, U$1-PWR.GND@B7, U$1-PWR.GND@B9, U$1-PWR.GND@C13, U$1-PWR.GND@C2, U$1-PWR.GND@C6, U$1-PWR.GND@C7, U$1-PWR.GND@C8, U$1-PWR.GND@C9, U$1-PWR.GND@D11, U$1-PWR.GND@D5, U$1-PWR.GND@D7, U$1-PWR.GND@D9, U$1-PWR.GND@E1, U$1-PWR.GND@E10, U$1-PWR.GND@E14, U$1-PWR.GND@E3, U$1-PWR.GND@E6, U$1-PWR.GND@E8, U$1-PWR.GND@F5, U$1-PWR.GND@F9, U$1-PWR.GND@G10, U$1-PWR.GND@G12, U$1-PWR.GND@G3, U$1-PWR.GND@G6, U$1-PWR.GND@H5, U$1-PWR.GND@H9, U$1-PWR.GND@J10, U$1-PWR.GND@J6, U$1-PWR.GND@K1, U$1-PWR.GND@K14, U$1-PWR.GND@K5, U$1-PWR.GND@K7, U$1-PWR.GND@K9, U$1-PWR.GND@L10, U$1-PWR.GND@L11, U$1-PWR.GND@L4, U$1-PWR.GND@L6, U$1-PWR.GND@L8, U$1-PWR.GND@N12, U$1-PWR.GND@N3, U$1-PWR.GND@N5, U$1-PWR.GND@N9, U$1-PWR.GND@P1, U$1-PWR.GND@P14, VREG1_0.GND@2; no longer AUX-SIO.6, C36.2, C73.2, C74.2, C75.2, C88.2, JP1.1, JP1.16, JP2.13, RESET_XLX.1, RESET_XLX.2, XLX-B0.IO_L1P_HSWAPEN_0, XLX-B2.IO_L13P_M1_2, XLX-BGND.GND@0, XLX-BGND.GND@1, XLX-BGND.GND@10, XLX-BGND.GND@11, XLX-BGND.GND@12, XLX-BGND.GND@2, XLX-BGND.GND@3, XLX-BGND.GND@4, XLX-BGND.GND@5, XLX-BGND.GND@6, XLX-BGND.GND@7, XLX-BGND.GND@8, XLX-BGND.GND@9, XLX-BNA.SUSPEND
- net HBUS_!REF!: no longer XLX-B2.IO_L62P_D5_2
- net HBUS_!RST!: no longer XLX-B2.IO_L49N_D4_2
- net HBUS_A0: no longer LVL_ALO.A1@3, XLX-B3.IO_L42P_GCLK25_TRDY2_3
- net HBUS_A1: no longer LVL_ALO.A2@4, XLX-B3.IO_L42N_GCLK24_3
- net HBUS_A10: no longer LVL_AHI.A3@5, XLX-B3.IO_L37N_3
- net HBUS_A11: no longer LVL_AHI.A4@6, XLX-B3.IO_L41P_GCLK27_3
- net HBUS_A12: no longer LVL_AHI.A5@7, XLX-B3.IO_L41N_GCLK26_3
- net HBUS_A13: no longer XLX-B3.IO_L2P_3
- net HBUS_A14: no longer XLX-B3.IO_L2N_3
- net HBUS_A15: no longer XLX-B3.IO_L36P_3
- net HBUS_A2: no longer LVL_ALO.A3@5, XLX-B3.IO_L43P_GCLK23_3
- net HBUS_A3: no longer LVL_ALO.A4@6, XLX-B3.IO_L43N_GCLK22_IRDY2_3
- net HBUS_A4: no longer LVL_ALO.A5@7, XLX-B3.IO_L44P_GCLK21_3
- net HBUS_A5: no longer LVL_ALO.A6@8, XLX-B3.IO_L44N_GCLK20_3
- net HBUS_A6: no longer LVL_ALO.A7@9, XLX-B3.IO_L49P_3
- net HBUS_A7: no longer LVL_ALO.A8@10, XLX-B3.IO_L49N_3
- net HBUS_A8: no longer LVL_AHI.A1@3, XLX-B3.IO_L36N_3
- net HBUS_A9: no longer LVL_AHI.A2@4, XLX-B3.IO_L37P_3
- net HBUS_CLK: no longer LVL_CLK.A@3, XLX-B3.IO_L1N_VREF_3
- net HBUS_D0: no longer LVL_D.A1@3, XLX-B3.IO_L50P_3
- net HBUS_D1: no longer LVL_D.A2@4, XLX-B3.IO_L50N_3
- net HBUS_D2: no longer LVL_D.A3@5, XLX-B3.IO_L51P_3
- net HBUS_D3: no longer LVL_D.A4@6, XLX-B3.IO_L51N_3
- net HBUS_D4: no longer LVL_D.A5@7, XLX-B3.IO_L52P_3
- net HBUS_D5: no longer LVL_D.A6@8, XLX-B3.IO_L52N_3
- net HBUS_D6: no longer LVL_D.A7@9, XLX-B3.IO_L83P_3
- net HBUS_D7: no longer LVL_D.A8@10, XLX-B3.IO_L83N_VREF_3
- net HBUS_R!W!: no longer LVL_RW.A@3, XLX-B2.IO_L49P_D3_2
- net HBUS_RD4: no longer XLX-B2.IO_L64P_D8_2
- net HBUS_RD5: no longer XLX-B2.IO_L62N_D6_2
- net HBUS_SIO_CLK: no longer XLX-B2.IO_L31N_GCLK30_D15_2
- net HBUS_SIO_CMD: no longer XLX-B2.IO_L31P_GCLK31_D14_2
- net HBUS_SIO_DIN: no longer XLX-B2.IO_L30N_GCLK0_USERCCLK_2
- net HBUS_SIO_DOUT: no longer XLX-B2.IO_L30P_GCLK1_D13_2
- net HBUS_SIO_MTR: no longer XLX-B2.IO_L14N_D12_2
- net LX_CLK: no longer XLX-B0.IO_L37P_GCLK13_0
- net LX_RC_N: now also U$1-B14.IO_L24N_T3_D16_14@P11; no longer XLX-B0.IO_L35N_GCLK16_0
- net LX_RC_P: now also U$1-B14.IO_L24P_T3_D17_14@P10; no longer XLX-B0.IO_L35P_GCLK17_0
- net LX_RD_N: now also U$1-B14.IO_L14N_T2_SRCC_14@H14; no longer XLX-B0.IO_L2N_0
- net LX_RD_P: now also U$1-B14.IO_L14P_T2_SRCC_14@H13; no longer XLX-B0.IO_L2P_0
- net LX_TC_N: now also U$1-B14.IO_L21N_T3_DQS_D22_14@M14; no longer XLX-B0.IO_L4N_0
- net LX_TC_P: now also U$1-B14.IO_L21P_T3_DQS_14@N14; no longer XLX-B0.IO_L4P_0
- net LX_TD0_N: now also U$1-B14.IO_L22N_T3_D20_14@P13; no longer XLX-B0.IO_L34N_GCLK18_0
- net LX_TD0_P: now also U$1-B14.IO_L22P_T3_D21_14@P12; no longer XLX-B0.IO_L34P_GCLK19_0
- net LX_TD1_N: now also U$1-B14.IO_L18N_T2_D27_14@J14; no longer XLX-B0.IO_L3N_0
- net LX_TD1_P: now also U$1-B14.IO_L18P_T2_D28_14@J13; no longer XLX-B0.IO_L3P_0
- net N$11: now also FPGA_PROG.SS/PROG/TMS@4, U$1-CFG.TMS_0@M6; no longer R81.1, XLX-B1.IO_L40N_GCLK10_1
- net N$48: now also FPGA_PROG.SCK/CCLK/TCK@6, U$1-CFG.TCK_0@A7; no longer FPGA_DONE.A, R52.2, XLX-B2.DONE_2
- net N$49: now also FPGA_PROG.MISO/DONE/TDO@8, U$1-CFG.TDO_0@P6; no longer R60.1, XLX-B2.IO_L65P_INIT_B_2
- net N$50: now also FPGA_PROG.MOSI/DIN/TDI@10, U$1-CFG.TDI_0@P7; no longer C30.1, R66.1, RESET_XLX.3, RESET_XLX.4, XLX-B2.PROGRAM_B_2
- net N$51: now also R52.1, U$1-CFG.CCLK_0@A8; no longer FPGA_PROG.SS/PROG/TMS@4, XLX-BNA.TMS
- net N$52: now also R60.1, U$1-CFG.IO_L6P_T0_FCS_B_14@C11; no longer FPGA_PROG.SCK/CCLK/TCK@6, XLX-BNA.TCK
- net N$55: now also R66.1, R68.2, U$1-CFG.DONE_0@P9; no longer FPGA_PROG.MISO/DONE/TDO@8, XLX-BNA.TDO
- net N$56: now also FPGA_DONE.A, R68.1; no longer FPGA_PROG.MOSI/DIN/TDI@10, XLX-BNA.TDI
- net N$69: now also R69.1, RESET_S7.3, RESET_S7.4, U$1-CFG.PROGRAM_B_0@L7; no longer R68.1, XLX-B2.IO_L1P_CCLK_2
- net N$7: now also C36.2, C73.2, C74.2, C75.2; no longer R82.1, XLX-B1.IO_L41N_GCLK8_1
- net N$70: now also R78.1, U$1-CFG.INIT_B_0@P8; no longer R69.1, XLX-B2.IO_L3N_MOSI_CSI_B_MISO0_2
- net N$77: now also U$1-CFG.CFGBVS_0@N7; no longer XLX-B1.IO_L33P_1
- net STMB0: no longer XIO-UNUSED.PB0@U5
- net STMB1: no longer XIO-UNUSED.PB1@T5
- net STMB12: no longer XIO-UNUSED.PB12@T14
- net STMB2: no longer XIO-UNUSED.PB2@R6
- net STMB6: no longer XIO-UNUSED.PB6@B5
- net STMB7: no longer XIO-UNUSED.PB7@C5
- net STMB8: no longer XIO-UNUSED.PB8@D5
- net STMB9: no longer XIO-UNUSED.PB9@D4
- net XSPI_3_MISO: no longer XLX-B1.IO_L41P_GCLK9_IRDY1_1
- net XSPI_3_MOSI: no longer R82.2
- net XSPI_3_SCK: no longer R81.2
- net XSPI_5_MISO: no longer XLX-B1.IO_L46N_1
- net XSPI_5_MOSI: no longer R87.2
- net XSPI_5_SCK: no longer R86.2
- net XSPI_6_MISO: no longer XLX-B1.IO_L32P_1
- net XSPI_6_MOSI: no longer R79.2
- net XSPI_6_SCK: no longer R78.2
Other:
- note added: "100uF 47uF 4.7uF 0.47uF"
- note added: "1210 caps can be placed anywhere 0805 caps within 2 electrical inches of part 0603 caps within 2 electrical inches of part"
- note added: ": GRM32ER60J107ME20L : GRM32ER70J476ME20L : GRM21BR71A475KA73 : GRM188R70J474KA01"
- note added: "Bypass cap number and capacitance taken from 483"
- note added: "Need to synchronise these two"
- note added: "No need for second 47uF"
- note added: "VccBram bypass caps"
- note added: "VccO bank 14"
- note added: "VccO bank 34"
- note removed: "Bank 0"
- note removed: "Bank 1"
- note removed: "Bypass cap number and capacitance taken from ug393"
- note removed: "CMPCS_B for Xilinx use only"
- note removed: "Clock"
- note removed: "Green LED"
- note removed: "Place 33R resistors close to FPGA pins"
- note removed: "VccO bank 0"
- note removed: "VccO bank 1"
- note removed: "VccO bank 2"
- note removed: "VccO bank 3"
